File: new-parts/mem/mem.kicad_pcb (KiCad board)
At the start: 2 copper layers, 101.6 x 101.6 mm, 15 parts, among them J1 BHR-10-VUA, J2 BHR-10-VUA, J3 Conn_01x02, K1 J104D2C12VDC.15S, U1 STM32F042C6Tx, U2 DRV8908

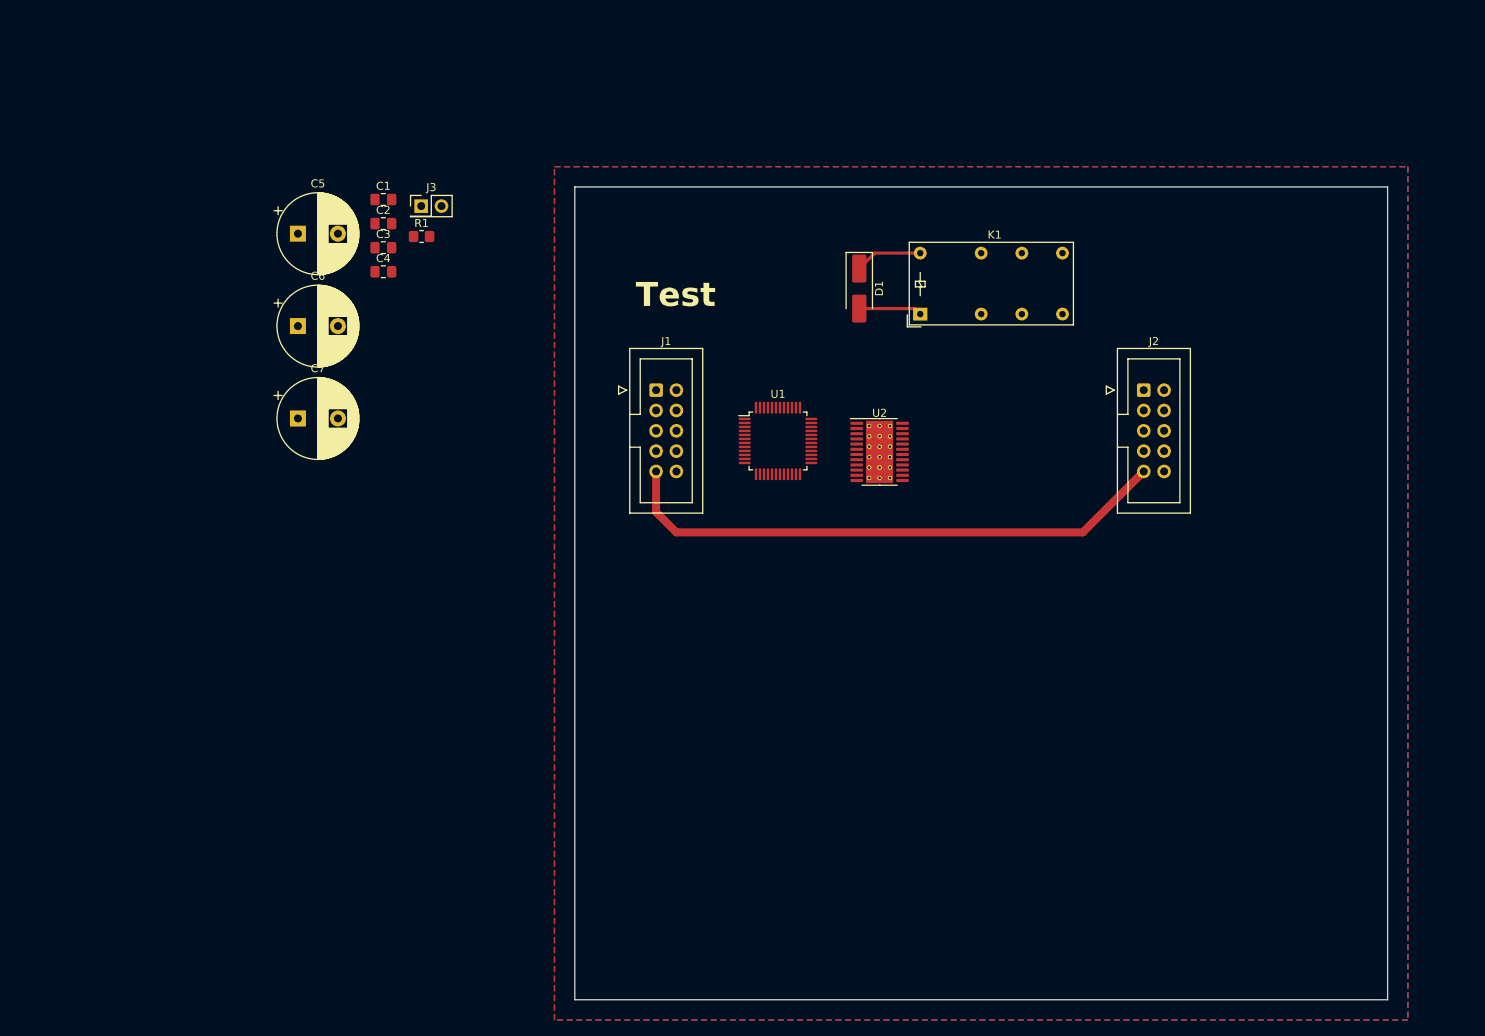
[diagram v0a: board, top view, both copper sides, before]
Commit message: Finish mem schematics and most of its layout.
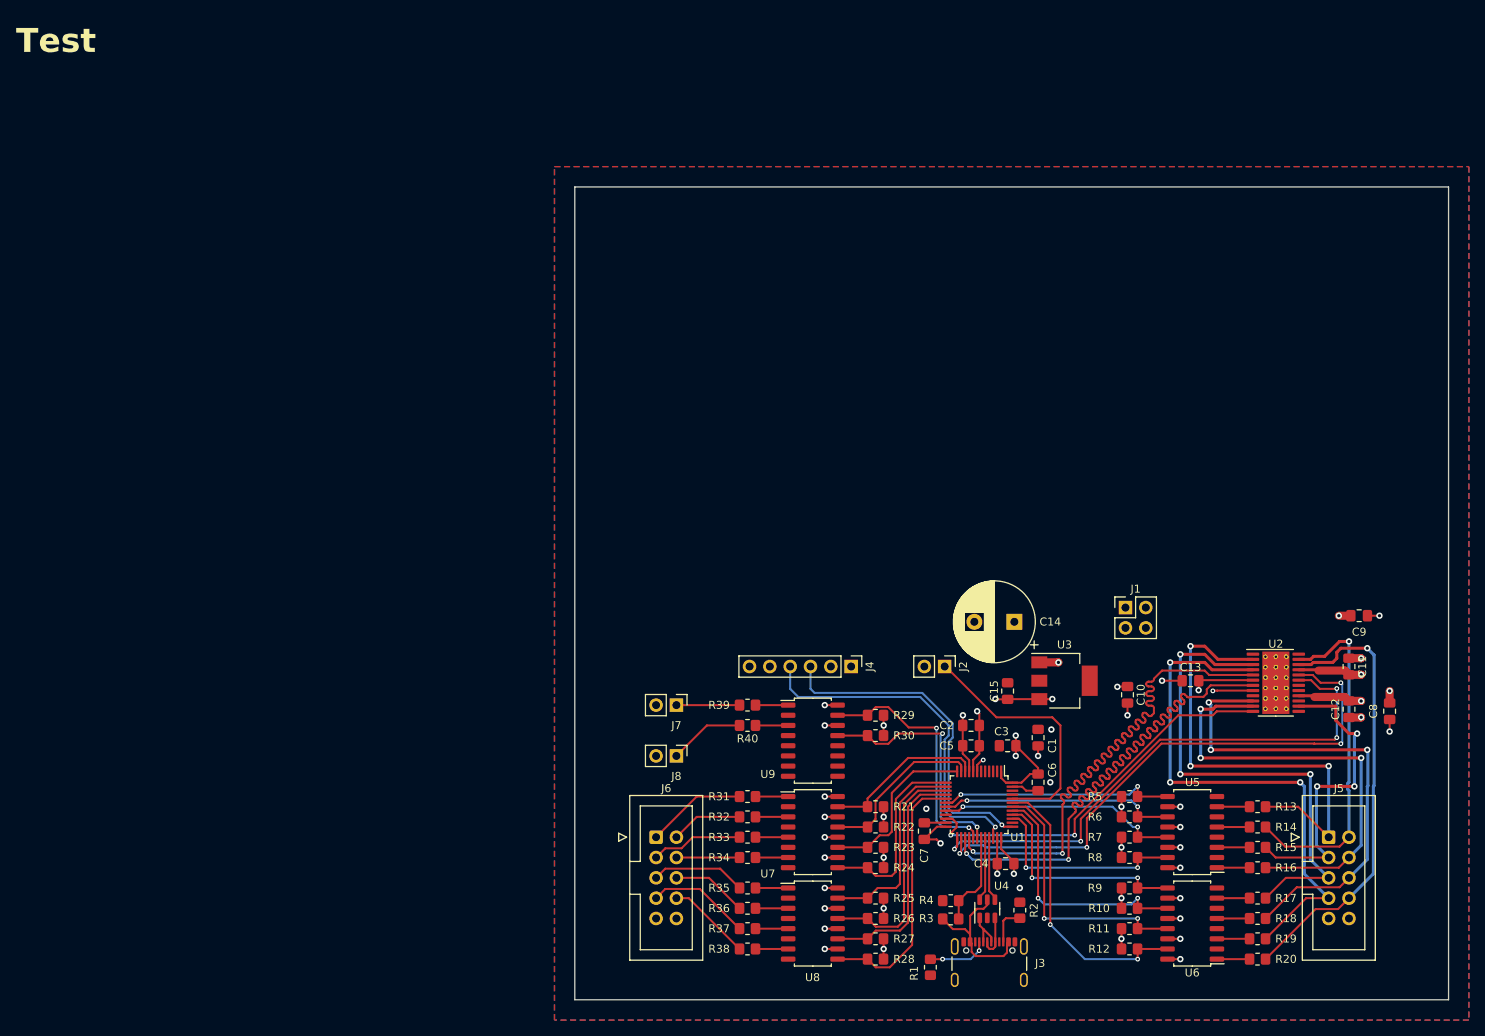
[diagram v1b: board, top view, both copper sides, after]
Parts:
- removed D1: SMAJ14CA, Diode_SMD:D_SMA_Handsoldering
- removed K1: J104D2C12VDC.15S, Relay_THT:Relay_DPDT_Finder_30.22
- added C10: 4.7u, Capacitor_SMD:C_0805_2012Metric_Pad1.18x1.45mm_HandSolder, F.Cu at (170.7, 114.3)
- added C11: 100n, Capacitor_SMD:C_0805_2012Metric_Pad1.18x1.45mm_HandSolder, F.Cu at (198.4, 110.7)
- added C12: 100n, Capacitor_SMD:C_0805_2012Metric_Pad1.18x1.45mm_HandSolder, F.Cu at (198.4, 116.1)
- added C13: 100n, Capacitor_SMD:C_0805_2012Metric_Pad1.18x1.45mm_HandSolder, F.Cu at (178.6, 112.5)
- added C14: 10u, Capacitor_THT:CP_Radial_D10.0mm_P5.00mm, F.Cu at (156.5, 105.2)
- added C15: 22u, Capacitor_SMD:C_0805_2012Metric_Pad1.18x1.45mm_HandSolder, F.Cu at (155.7, 113.8)
- added C8: 4.7u, Capacitor_SMD:C_0805_2012Metric_Pad1.18x1.45mm_HandSolder, F.Cu at (203.5, 116.3)
- added C9: 4.7u, Capacitor_SMD:C_0805_2012Metric_Pad1.18x1.45mm_HandSolder, F.Cu at (199.6, 104.4)
- added J1: Conn_02x02_Odd_Even, Connector_PinHeader_2.54mm:PinHeader_2x02_P2.54mm_Vertical, F.Cu at (170.4, 103.4)
- added J4: Conn_01x06, Connector_PinHeader_2.54mm:PinHeader_1x06_P2.54mm_Vertical, F.Cu at (136.1, 110.7)
- added J5: BHR-10-VUA, Connector_IDC:IDC-Header_2x05_P2.54mm_Vertical, F.Cu at (195.8, 132.1)
- added J7: Conn_02x01, Connector_PinHeader_2.54mm:PinHeader_1x02_P2.54mm_Vertical, F.Cu at (114.3, 115.6)
- added J8: Conn_02x01, Connector_PinHeader_2.54mm:PinHeader_1x02_P2.54mm_Vertical, F.Cu at (114.3, 121.9)
- added R10: 10k, Resistor_SMD:R_0805_2012Metric_Pad1.20x1.40mm_HandSolder, F.Cu at (170.9, 141.0)
- added R11: 10k, Resistor_SMD:R_0805_2012Metric_Pad1.20x1.40mm_HandSolder, F.Cu at (170.9, 143.5)
- added R12: 10k, Resistor_SMD:R_0805_2012Metric_Pad1.20x1.40mm_HandSolder, F.Cu at (170.9, 146.1)
- added R13: 2.2k, Resistor_SMD:R_0805_2012Metric_Pad1.20x1.40mm_HandSolder, F.Cu at (186.9, 128.3)
- added R14: 2.2k, Resistor_SMD:R_0805_2012Metric_Pad1.20x1.40mm_HandSolder, F.Cu at (186.9, 130.8)
- added R15: 2.2k, Resistor_SMD:R_0805_2012Metric_Pad1.20x1.40mm_HandSolder, F.Cu at (186.9, 133.3)
- added R16: 2.2k, Resistor_SMD:R_0805_2012Metric_Pad1.20x1.40mm_HandSolder, F.Cu at (186.9, 135.9)
- added R17: 2.2k, Resistor_SMD:R_0805_2012Metric_Pad1.20x1.40mm_HandSolder, F.Cu at (186.9, 139.7)
- added R18: 2.2k, Resistor_SMD:R_0805_2012Metric_Pad1.20x1.40mm_HandSolder, F.Cu at (186.9, 142.2)
- added R19: 2.2k, Resistor_SMD:R_0805_2012Metric_Pad1.20x1.40mm_HandSolder, F.Cu at (186.9, 144.8)
- added R2: 5.1k, Resistor_SMD:R_0805_2012Metric_Pad1.20x1.40mm_HandSolder, F.Cu at (157.2, 141.2)
- added R20: 2.2k, Resistor_SMD:R_0805_2012Metric_Pad1.20x1.40mm_HandSolder, F.Cu at (186.9, 147.3)
- added R21: 10k, Resistor_SMD:R_0805_2012Metric_Pad1.20x1.40mm_HandSolder, F.Cu at (139.2, 128.3)
- added R22: 10k, Resistor_SMD:R_0805_2012Metric_Pad1.20x1.40mm_HandSolder, F.Cu at (139.2, 130.8)
- added R23: 10k, Resistor_SMD:R_0805_2012Metric_Pad1.20x1.40mm_HandSolder, F.Cu at (139.2, 133.3)
- added R24: 10k, Resistor_SMD:R_0805_2012Metric_Pad1.20x1.40mm_HandSolder, F.Cu at (139.2, 135.9)
- added R25: 10k, Resistor_SMD:R_0805_2012Metric_Pad1.20x1.40mm_HandSolder, F.Cu at (139.2, 139.7)
- added R26: 10k, Resistor_SMD:R_0805_2012Metric_Pad1.20x1.40mm_HandSolder, F.Cu at (139.2, 142.2)
- added R27: 10k, Resistor_SMD:R_0805_2012Metric_Pad1.20x1.40mm_HandSolder, F.Cu at (139.2, 144.8)
- added R28: 10k, Resistor_SMD:R_0805_2012Metric_Pad1.20x1.40mm_HandSolder, F.Cu at (139.2, 147.3)
- added R29: 10k, Resistor_SMD:R_0805_2012Metric_Pad1.20x1.40mm_HandSolder, F.Cu at (139.2, 116.8)
- added R3: 33k, Resistor_SMD:R_0805_2012Metric_Pad1.20x1.40mm_HandSolder, F.Cu at (148.6, 142.3)
- added R30: 10k, Resistor_SMD:R_0805_2012Metric_Pad1.20x1.40mm_HandSolder, F.Cu at (139.2, 119.4)
- added R31: 2.2k, Resistor_SMD:R_0805_2012Metric_Pad1.20x1.40mm_HandSolder, F.Cu at (123.2, 127.0)
- added R32: 2.2k, Resistor_SMD:R_0805_2012Metric_Pad1.20x1.40mm_HandSolder, F.Cu at (123.2, 129.5)
- added R33: 2.2k, Resistor_SMD:R_0805_2012Metric_Pad1.20x1.40mm_HandSolder, F.Cu at (123.2, 132.1)
- added R34: 2.2k, Resistor_SMD:R_0805_2012Metric_Pad1.20x1.40mm_HandSolder, F.Cu at (123.2, 134.6)
- added R35: 2.2k, Resistor_SMD:R_0805_2012Metric_Pad1.20x1.40mm_HandSolder, F.Cu at (123.2, 138.4)
- added R36: 2.2k, Resistor_SMD:R_0805_2012Metric_Pad1.20x1.40mm_HandSolder, F.Cu at (123.2, 141.0)
- added R37: 2.2k, Resistor_SMD:R_0805_2012Metric_Pad1.20x1.40mm_HandSolder, F.Cu at (123.2, 143.5)
- added R38: 2.2k, Resistor_SMD:R_0805_2012Metric_Pad1.20x1.40mm_HandSolder, F.Cu at (123.2, 146.1)
- added R39: 2.2k, Resistor_SMD:R_0805_2012Metric_Pad1.20x1.40mm_HandSolder, F.Cu at (123.2, 115.6)
- added R4: 82k, Resistor_SMD:R_0805_2012Metric_Pad1.20x1.40mm_HandSolder, F.Cu at (148.6, 140.0)
- added R40: 2.2k, Resistor_SMD:R_0805_2012Metric_Pad1.20x1.40mm_HandSolder, F.Cu at (123.2, 118.1)
- added R5: 10k, Resistor_SMD:R_0805_2012Metric_Pad1.20x1.40mm_HandSolder, F.Cu at (170.9, 127.0)
- added R6: 10k, Resistor_SMD:R_0805_2012Metric_Pad1.20x1.40mm_HandSolder, F.Cu at (170.9, 129.5)
- added R7: 10k, Resistor_SMD:R_0805_2012Metric_Pad1.20x1.40mm_HandSolder, F.Cu at (170.9, 132.1)
- added R8: 10k, Resistor_SMD:R_0805_2012Metric_Pad1.20x1.40mm_HandSolder, F.Cu at (170.9, 134.6)
- added R9: 10k, Resistor_SMD:R_0805_2012Metric_Pad1.20x1.40mm_HandSolder, F.Cu at (170.9, 138.4)
- added U3: AZ1117H2-3.3, Package_TO_SOT_SMD:SOT-223-3_TabPin2, F.Cu at (162.8, 112.5)
- added U4: USBLC6-2SC6, Package_TO_SOT_SMD:SOT-23-6, F.Cu at (153.2, 141.0)
- added U5: LTV-247, Package_SO:SOP-16_4.4x10.4mm_P1.27mm, F.Cu at (178.8, 131.4)
- added U6: LTV-247, Package_SO:SOP-16_4.4x10.4mm_P1.27mm, F.Cu at (178.8, 142.9)
- added U7: LTV-247, Package_SO:SOP-16_4.4x10.4mm_P1.27mm, F.Cu at (131.4, 131.4)
- added U8: LTV-247, Package_SO:SOP-16_4.4x10.4mm_P1.27mm, F.Cu at (131.4, 142.9)
- added U9: LTV-247, Package_SO:SOP-16_4.4x10.4mm_P1.27mm, F.Cu at (131.4, 120.0)
- C1: renamed from C7; footprint Capacitor_THT:CP_Radial_D10.0mm_P5.00mm -> Capacitor_SMD:C_0805_2012Metric_Pad1.18x1.45mm_HandSolder
- C2: renamed from C6; footprint Capacitor_THT:CP_Radial_D10.0mm_P5.00mm -> Capacitor_SMD:C_0805_2012Metric_Pad1.18x1.45mm_HandSolder
- C3: renamed from C5; footprint Capacitor_THT:CP_Radial_D10.0mm_P5.00mm -> Capacitor_SMD:C_0805_2012Metric_Pad1.18x1.45mm_HandSolder
- J2: value BHR-10-VUA -> Conn_02x01; footprint Connector_IDC:IDC-Header_2x05_P2.54mm_Vertical -> Connector_PinHeader_2.54mm:PinHeader_1x02_P2.54mm_Vertical
- J3: value Conn_01x02 -> USB_C_Receptacle_USB2.0; footprint Connector_PinHeader_2.54mm:PinHeader_2x01_P2.54mm_Vertical -> Connector_USB:USB_C_Receptacle_GCT_USB4105-xx-A_16P_TopMnt_Horizontal
- R1: value 10k -> 5.1k
- moved J3 119.1 mm to (153.4, 148.8)
- moved R1 111.3 mm to (146.1, 148.3), turned to -90 degrees
- moved C3 109.4 mm to (155.7, 120.7), turned to 180 degrees
- moved C6 107.6 mm to (159.5, 125.2), turned to 90 degrees
- moved C4 107.3 mm to (155.4, 135.4)
- moved C7 103.9 mm to (145.3, 131.3), turned to -90 degrees
- moved C1 100.8 mm to (159.5, 119.6), turned to 90 degrees
- moved C2 97.8 mm to (151.1, 118.1)
- moved C5 96.3 mm to (151.1, 120.7), turned to 180 degrees
- moved U2 57.3 mm to (189.2, 112.8)
- moved J6 55.9 mm to (111.8, 132.1)
- moved U1 52.0 mm to (152.1, 128.0), turned to -90 degrees
- moved J2 42.6 mm to (147.8, 110.7), turned to -90 degrees
- renumbered C3 to C5, C2 to C6, C1 to C7, J1 to J6
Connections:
- J2 pad 1: unconnected-(J2-Pin_1-Pad1) -> /boot0
- J2 pad 2: unconnected-(J2-Pin_2-Pad2) -> GND
- J6 pad 1: unconnected-(J1-Pin_1-Pad1) -> Net-(J6-Pin_1)
- J6 pad 2: unconnected-(J1-Pin_2-Pad2) -> Net-(J6-Pin_2)
- J6 pad 3: unconnected-(J1-Pin_3-Pad3) -> Net-(J6-Pin_3)
- J6 pad 4: unconnected-(J1-Pin_4-Pad4) -> Net-(J6-Pin_4)
- J6 pad 5: unconnected-(J1-Pin_5-Pad5) -> Net-(J6-Pin_5)
- J6 pad 6: unconnected-(J1-Pin_6-Pad6) -> Net-(J6-Pin_6)
- J6 pad 7: unconnected-(J1-Pin_7-Pad7) -> Net-(J6-Pin_7)
- J6 pad 8: unconnected-(J1-Pin_8-Pad8) -> Net-(J6-Pin_8)
- R1 pad 1: +3V3 -> Net-(J3-CC1)
- R1 pad 2: Net-(J3-Pin_1) -> GND
- U1 pad 1: unconnected-(U1-VBAT-Pad1) -> +3V3
- U1 pad 22: unconnected-(U1-PB11-Pad22) -> /~{fault}
- U1 pad 31: unconnected-(U1-PA10-Pad31) -> /vbus_sense
- U1 pad 32: /usb_dm -> /usb_dN
- U1 pad 33: /usb_dp -> /usb_dP
- U1 pad 44: unconnected-(U1-PF11-Pad44) -> /boot0
- U1 pad 7: Net-(J3-Pin_1) -> /~{rst}
- U2 pad 10: unconnected-(U2-OUT6-Pad10) -> /out5
- U2 pad 11: unconnected-(U2-OUT4-Pad11) -> /out3
- U2 pad 12: unconnected-(U2-~{FAULT}-Pad12) -> /~{fault}
- U2 pad 14: unconnected-(U2-OUT3-Pad14) -> /out2
- U2 pad 2: unconnected-(U2-OUT1-Pad2) -> /out0
- U2 pad 22: unconnected-(U2-OUT8-Pad22) -> /out7
- U2 pad 23: unconnected-(U2-OUT2-Pad23) -> /out1
- U2 pad 25: (no net) -> GND
- U2 pad 3: unconnected-(U2-OUT5-Pad3) -> /out4
- U2 pad 4: unconnected-(U2-OUT7-Pad4) -> /out6
- U2 pad 8: unconnected-(U2-~{SLEEP}-Pad8) -> +3V3
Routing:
- net +3V3: track 0.00 -> 123.4 mm, vias 0 -> 29
- net /mosi: track 0.00 -> 74.6 mm, vias 0 -> 2
- net /miso: track 0.00 -> 74.5 mm, vias 0 -> 2
- net /sclk: track 0.00 -> 71.2 mm, vias 0 -> 4
- net /~{cs}: track 0.00 -> 68.2 mm, vias 0 -> 4
- net /out6: track 0.00 -> 67.9 mm, vias 0 -> 3
- net /out4: track 0.00 -> 63.7 mm, vias 0 -> 3
- net /out5: track 0.00 -> 60.7 mm, vias 0 -> 3
- net /out0: track 0.00 -> 59.1 mm, vias 0 -> 3
- net /out3: track 0.00 -> 56.9 mm, vias 0 -> 3
- net /out7: track 0.00 -> 56.3 mm, vias 0 -> 1
- net GND: track 0.00 -> 51.6 mm, vias 0 -> 21
- net /~{fault}: track 0.00 -> 48.8 mm, vias 0 -> 2
- net +12V: track 70.2 -> 21.6 mm, vias 0 -> 5
- net /swdio: track 0.00 -> 44.1 mm, vias 0 -> 1
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- added copper zone on In1.Cu, net +12V
- added copper zone on In1.Cu, net +3V3
- added copper zone on In2.Cu, net GND
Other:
- board size 101.6 x 101.6 mm -> 109.2 x 101.6 mm
- copper layers 2 -> 4
